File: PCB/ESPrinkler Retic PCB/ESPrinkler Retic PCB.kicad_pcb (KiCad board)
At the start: 2 copper layers, 120.4 x 85.7 mm, 158 parts, among them J4 Conn_01x19, J5 Conn_01x19, J6 Conn_01x04, Q1 AO3400A, Q10 AO3400A, Q11 AO3400A, Q2 AO3400A, Q3 AO3400A, Q4 AO3400A, Q5 AO3400A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

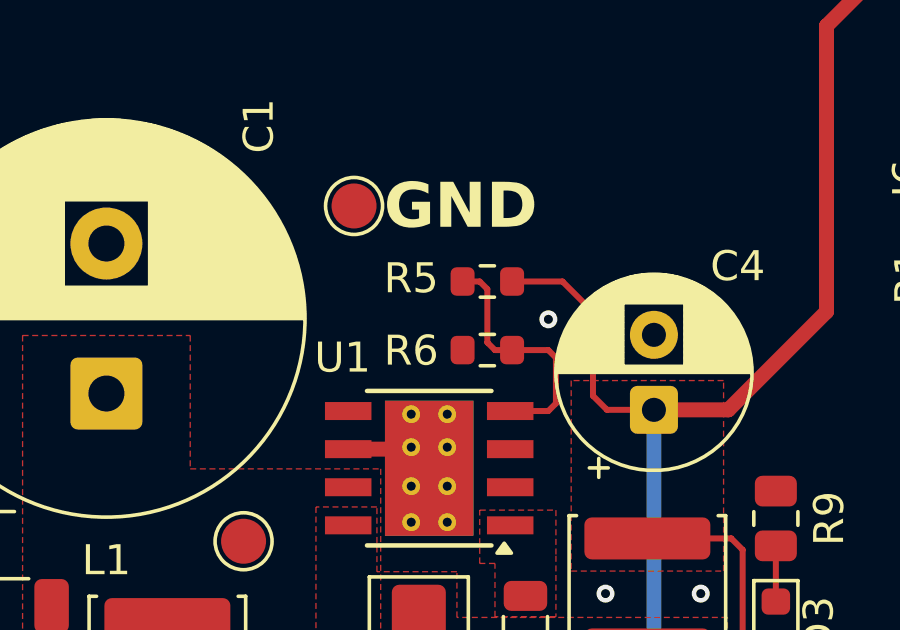
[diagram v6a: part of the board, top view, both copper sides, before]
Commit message: Change SMPS voltage divider
Somehow managed to miscalculate the voltage divider resistor values to get 5V, getting 7V.

Change resistor values, change to 0805 footprint.
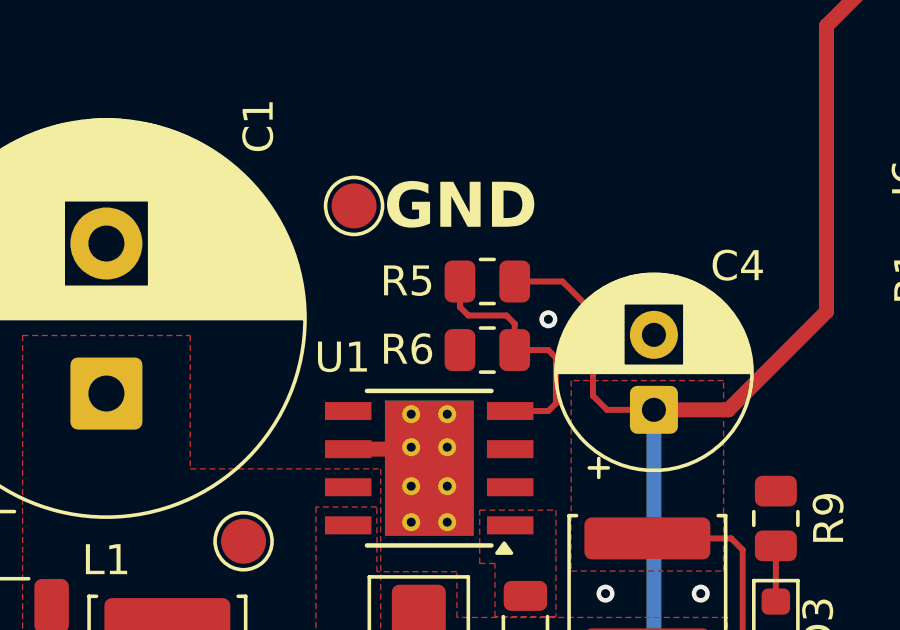
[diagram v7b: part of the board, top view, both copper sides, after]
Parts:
- R5: value 53.6k -> 10k; footprint Resistor_SMD:R_0603_1608Metric -> Resistor_SMD:R_0805_2012Metric
- R6: value 10.2k -> 3.24k; footprint Resistor_SMD:R_0603_1608Metric -> Resistor_SMD:R_0805_2012Metric
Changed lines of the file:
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@@
 		(embedded_fonts no)
 	)
-	(footprint "Resistor_SMD:R_0603_1608Metric"
+	(footprint "Resistor_SMD:R_0805_2012Metric"
 		(layer "F.Cu")
 		(at 153.414 82.179 180)
-		(descr "Resistor SMD 0603 (1608 Metric), square (rectangular) end terminal, IPC-7351 nominal, (Body size source: IPC-SM-782 page 72, https://www.pcb-3d.com/wordpress/wp-content/uploads/ipc-sm-782a_amendment_1_and_2.pdf), generated with kicad-footprint-generator")
+		(descr "Resistor SMD 0805 (2012 Metric), square (rectangular) end terminal, IPC-7351 nominal, (Body size source: IPC-SM-782 page 72, https://www.pcb-3d.com/wordpress/wp-content/uploads/ipc-sm-782a_amendment_1_and_2.pdf), generated with kicad-footprint-generator")
 		(tags "resistor")
 		(property "Reference" "R6"
-			(at 2.538 -0.022 180)
+			(at 2.665 0.01 180)
 			(layer "F.SilkS")
 			(effects
@@
 			)
 		)
-		(property "Value" "10.2k"
-			(at 0 1.43 180)
+		(property "Value" "3.24k"
+			(at 0 1.65 180)
 			(layer "F.Fab")
 			(effects
@@
 			)
 		)
-		(property "Description" "Resistor"
+		(property "Description" "125mW Thick Film Resistor 150V ±100ppm/℃ ±1% 3.24kΩ 0805 Chip Resistor - Surface Mount ROHS"
 			(at 0 0 180)
 			(layer "F.Fab")
@@
 			)
 		)
-		(property "Manufacturer P/N" "0603WAF1022T5E"
+		(property "Manufacturer P/N" "0805W8F3241T5E"
 			(at 0 0 180)
 			(unlocked yes)
@@
 			)
 		)
-		(property "Supplier P/N" "C22772"
+		(property "Supplier P/N" "C17609"
 			(at 0 0 180)
 			(unlocked yes)
@@
 		(attr smd)
 		(fp_line
-			(start -0.237258 0.5225)
-			(end 0.237258 0.5225)
+			(start -0.227064 0.735)
+			(end 0.227064 0.735)
 			(stroke
 				(width 0.12)
@@
 		)
 		(fp_line
-			(start -0.237258 -0.5225)
-			(end 0.237258 -0.5225)
+			(start -0.227064 -0.735)
+			(end 0.227064 -0.735)
 			(stroke
 				(width 0.12)
@@
 		)
 		(fp_line
-			(start 1.48 0.73)
-			(end -1.48 0.73)
+			(start 1.68 0.95)
+			(end -1.68 0.95)
 			(stroke
 				(width 0.05)
@@
 		)
 		(fp_line
-			(start 1.48 -0.73)
-			(end 1.48 0.73)
+			(start 1.68 -0.95)
+			(end 1.68 0.95)
 			(stroke
 				(width 0.05)
@@
 		)
 		(fp_line
-			(start -1.48 0.73)
-			(end -1.48 -0.73)
+			(start -1.68 0.95)
+			(end -1.68 -0.95)
 			(stroke
 				(width 0.05)
@@
 		)
 		(fp_line
-			(start -1.48 -0.73)
-			(end 1.48 -0.73)
+			(start -1.68 -0.95)
+			(end 1.68 -0.95)
 			(stroke
 				(width 0.05)
@@
 		)
 		(fp_line
-			(start 0.8 0.4125)
-			(end -0.8 0.4125)
+			(start 1 0.625)
+			(end -1 0.625)
 			(stroke
 				(width 0.1)
@@
 		)
 		(fp_line
-			(start 0.8 -0.4125)
-			(end 0.8 0.4125)
+			(start 1 -0.625)
+			(end 1 0.625)
 			(stroke
 				(width 0.1)
@@
 		)
 		(fp_line
-			(start -0.8 0.4125)
-			(end -0.8 -0.4125)
+			(start -1 0.625)
+			(end -1 -0.625)
 			(stroke
 				(width 0.1)
@@
 		)
 		(fp_line
-			(start -0.8 -0.4125)
-			(end 0.8 -0.4125)
+			(start -1 -0.625)
+			(end 1 -0.625)
 			(stroke
 				(width 0.1)
@@
 			(effects
 				(font
-					(size 0.4 0.4)
-					(thickness 0.06)
+					(size 0.5 0.5)
+					(thickness 0.08)
 				)
 			)
 		)
 		(pad "1" smd roundrect
-			(at -0.825 0 180)
-			(size 0.8 0.95)
+			(at -0.9125 0 180)
+			(size 1.025 1.4)
 			(layers "F.Cu" "F.Mask" "F.Paste")
-			(roundrect_rratio 0.25)
+			(roundrect_rratio 0.243902)
 			(net 95 "Net-(U1-VSENSE)")
 			(pintype "passive")
 		)
 		(pad "2" smd roundrect
-			(at 0.825 0 180)
-			(size 0.8 0.95)
+			(at 0.9125 0 180)
+			(size 1.025 1.4)
 			(layers "F.Cu" "F.Mask" "F.Paste")
-			(roundrect_rratio 0.25)
+			(roundrect_rratio 0.243902)
 			(net 2 "GND")
 			(pintype "passive")
 		)
 		(embedded_fonts no)
-		(model "${KICAD9_3DMODEL_DIR}/Resistor_SMD.3dshapes/R_0603_1608Metric.step"
+		(model "${KICAD9_3DMODEL_DIR}/Resistor_SMD.3dshapes/R_0805_2012Metric.step"
 			(offset
 				(xyz 0 0 0)
@@
 		)
 	)
-	(footprint "Resistor_SMD:R_0603_1608Metric"
+	(footprint "Resistor_SMD:R_0805_2012Metric"
 		(layer "F.Cu")
 		(at 153.414 79.893 180)
-		(descr "Resistor SMD 0603 (1608 Metric), square (rectangular) end terminal, IPC-7351 nominal, (Body size source: IPC-SM-782 page 72, https://www.pcb-3d.com/wordpress/wp-content/uploads/ipc-sm-782a_amendment_1_and_2.pdf), generated with kicad-footprint-generator")
+		(descr "Resistor SMD 0805 (2012 Metric), square (rectangular) end terminal, IPC-7351 nominal, (Body size source: IPC-SM-782 page 72, https://www.pcb-3d.com/wordpress/wp-content/uploads/ipc-sm-782a_amendment_1_and_2.pdf), generated with kicad-footprint-generator")
 		(tags "resistor")
 		(property "Reference" "R5"
-			(at 2.538 0.105 180)
+			(at 2.665 0 180)
 			(layer "F.SilkS")
 			(effects
@@
 			)
 		)
-		(property "Value" "53.6k"
-			(at 0 1.43 180)
+		(property "Value" "10k"
+			(at 0 1.65 180)
 			(layer "F.Fab")
 			(effects
@@
 			)
 		)
-		(property "Manufacturer P/N" "0603WAF5362T5E"
+		(property "Manufacturer P/N" "0805W8F1002T5E"
 			(at 0 0 180)
 			(unlocked yes)
@@
 			)
 		)
-		(property "Supplier P/N" "C23074"
+		(property "Supplier P/N" "C17414"
 			(at 0 0 180)
 			(unlocked yes)
@@
 		(attr smd)
 		(fp_line
-			(start -0.237258 0.5225)
-			(end 0.237258 0.5225)
+			(start -0.227064 0.735)
+			(end 0.227064 0.735)
 			(stroke
 				(width 0.12)
@@
 		)
 		(fp_line
-			(start -0.237258 -0.5225)
-			(end 0.237258 -0.5225)
+			(start -0.227064 -0.735)
+			(end 0.227064 -0.735)
 			(stroke
 				(width 0.12)
@@
 		)
 		(fp_line
-			(start 1.48 0.73)
-			(end -1.48 0.73)
+			(start 1.68 0.95)
+			(end -1.68 0.95)
 			(stroke
 				(width 0.05)
@@
 		)
 		(fp_line
-			(start 1.48 -0.73)
-			(end 1.48 0.73)
+			(start 1.68 -0.95)
+			(end 1.68 0.95)
 			(stroke
 				(width 0.05)
@@
 		)
 		(fp_line
-			(start -1.48 0.73)
-			(end -1.48 -0.73)
+			(start -1.68 0.95)
+			(end -1.68 -0.95)
 			(stroke
 				(width 0.05)
@@
 		)
 		(fp_line
-			(start -1.48 -0.73)
-			(end 1.48 -0.73)
+			(start -1.68 -0.95)
+			(end 1.68 -0.95)
 			(stroke
 				(width 0.05)
@@
 		)
 		(fp_line
-			(start 0.8 0.4125)
-			(end -0.8 0.4125)
+			(start 1 0.625)
+			(end -1 0.625)
 			(stroke
 				(width 0.1)
@@
 		)
 		(fp_line
-			(start 0.8 -0.4125)
-			(end 0.8 0.4125)
+			(start 1 -0.625)
+			(end 1 0.625)
 			(stroke
 				(width 0.1)
@@
 		)
 		(fp_line
-			(start -0.8 0.4125)
-			(end -0.8 -0.4125)
+			(start -1 0.625)
+			(end -1 -0.625)
 			(stroke
 				(width 0.1)
@@
 		)
 		(fp_line
-			(start -0.8 -0.4125)
-			(end 0.8 -0.4125)
+			(start -1 -0.625)
+			(end 1 -0.625)
 			(stroke
 				(width 0.1)
@@
 			(effects
 				(font
-					(size 0.4 0.4)
-					(thickness 0.06)
+					(size 0.5 0.5)
+					(thickness 0.08)
 				)
 			)
 		)
 		(pad "1" smd roundrect
-			(at -0.825 0 180)
-			(size 0.8 0.95)
+			(at -0.9125 0 180)
+			(size 1.025 1.4)
 			(layers "F.Cu" "F.Mask" "F.Paste")
-			(roundrect_rratio 0.25)
+			(roundrect_rratio 0.243902)
 			(net 5 "+5V")
 			(pintype "passive")
 		)
 		(pad "2" smd roundrect
-			(at 0.825 0 180)
-			(size 0.8 0.95)
+			(at 0.9125 0 180)
+			(size 1.025 1.4)
 			(layers "F.Cu" "F.Mask" "F.Paste")
-			(roundrect_rratio 0.25)
+			(roundrect_rratio 0.243902)
 			(net 95 "Net-(U1-VSENSE)")
 			(pintype "passive")
 		)
 		(embedded_fonts no)
-		(model "${KICAD9_3DMODEL_DIR}/Resistor_SMD.3dshapes/R_0603_1608Metric.step"
+		(model "${KICAD9_3DMODEL_DIR}/Resistor_SMD.3dshapes/R_0805_2012Metric.step"
 			(offset
 				(xyz 0 0 0)
@@
 	)
 	(segment
-		(start 153.668 82.179)
-		(end 153.414 81.925)
+		(start 152.5015 80.7465)
+		(end 152.5015 79.893)
 		(width 0.2)
 		(layer "F.Cu")
@@
 	)
 	(segment
-		(start 154.176 84.211)
-		(end 155.446 84.211)
+		(start 154.051 81.026)
+		(end 152.781 81.026)
 		(width 0.2)
 		(layer "F.Cu")
@@
 	)
 	(segment
-		(start 155.7 82.433)
-		(end 155.446 82.179)
+		(start 154.176 84.211)
+		(end 155.446 84.211)
 		(width 0.2)
 		(layer "F.Cu")
@@
 	)
 	(segment
-		(start 155.446 82.179)
-		(end 154.3265 82.179)
+		(start 154.3265 81.3015)
+		(end 154.051 81.026)
 		(width 0.2)
 		(layer "F.Cu")
@@
 	)
 	(segment
-		(start 155.446 84.211)
-		(end 155.7 83.957)
+		(start 154.3265 82.179)
+		(end 154.3265 81.3015)
 		(width 0.2)
 		(layer "F.Cu")
@@
 	)
 	(segment
-		(start 153.414 81.925)
-		(end 153.414 80.147)
+		(start 155.7 82.433)
+		(end 155.446 82.179)
 		(width 0.2)
 		(layer "F.Cu")
@@
 	)
 	(segment
-		(start 154.3265 82.179)
-		(end 153.668 82.179)
+		(start 152.781 81.026)
+		(end 152.5015 80.7465)
 		(width 0.2)
 		(layer "F.Cu")
@@
 	)
 	(segment
-		(start 155.7 83.957)
-		(end 155.7 82.433)
+		(start 155.446 82.179)
+		(end 154.3265 82.179)
 		(width 0.2)
 		(layer "F.Cu")
@@
 	)
 	(segment
-		(start 153.414 80.147)
-		(end 153.16 79.893)
+		(start 155.446 84.211)
+		(end 155.7 83.957)
 		(width 0.2)
 		(layer "F.Cu")
@@
 	)
 	(segment
-		(start 153.16 79.893)
-		(end 152.5015 79.893)
+		(start 155.7 83.957)
+		(end 155.7 82.433)
 		(width 0.2)
 		(layer "F.Cu")
